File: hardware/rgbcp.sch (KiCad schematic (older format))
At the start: 139 parts, among them SW0 SW_PUSH, SW1 SW_PUSH, SW2 SW_PUSH, SW3 SW_PUSH, SW4 SW_PUSH, SW5 SW_PUSH

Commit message: fix #4: Part List For Schematic
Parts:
- removed U?: MAX603ESA, symbol MAX603ESA
- gave numbers to parts that had none: 70
- renumbered SW0 to B0, SW1 to B1, SW2 to B2, SW3 to B3, SW4 to B4, SW5 to B5, BAT1 to BH1, BAT2 to BH2, BAT3 to BH3, BAT4 to BH4, CXTAL1 to C3, CXTAL2 to C4, DUSB to D1, FETPOL to F1, FETTYP to F2, FETBT1 to F3, FETBT2 to F4, LEDBAT0 to L0, LED0_1 to L0_1, LED0_2 to L0_2, LED0_3 to L0_3, LEDBAT1 to L1, LED1_1 to L1_1, LED1_2 to L1_2, LED1_3 to L1_3, LEDBAT2 to L2, LED2_1 to L2_1, LED2_2 to L2_2, LED2_3 to L2_3, LEDBAT3 to L3, LED3_1 to L3_1, LED3_2 to L3_2, LED3_3 to L3_3, LEDDBG to L4, LED4_1 to L4_1, LED4_2 to L4_2, LED4_3 to L4_3, LED5_1 to L5_1, LED5_2 to L5_2, LED5_3 to L5_3, LED6_1 to L6_1, LED6_2 to L6_2, LED6_3 to L6_3, LED7_1 to L7_1, LED7_2 to L7_2, LED7_3 to L7_3, LED8_1 to L8_1, LED8_2 to L8_2, LED8_3 to L8_3, LED9_1 to L9_1, LED9_2 to L9_2, LED9_3 to L9_3, BJTCS0 to Q0, BJTCS1 to Q1, BJTCS2 to Q2, BJTCS3 to Q3, BJTCS4 to Q4, BJTCS5 to Q5, BJTCS6 to Q6, BJTCS7 to Q7, BJTCS8 to Q8, BJTCS9 to Q9, JUSB to S1, JPBAT to SW1, JPFLAG to SW2, UMCU to U1, ULDO to U2, XTAL to X1
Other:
- note added: "Automatic Power Supply Selector"
- note added: "Battery Level"
- note added: "Debug LEDs"
- note added: "Debug Switches"
- note added: "LEDs for Battery Level"
- note added: "Power Supply (3.3V) for MCU"
- note added: "Power Supply (4V) for all LEDs"
- note added: "Power \nSupply \nStatus"
- note added: "Reverse \nBattery \nProtection"

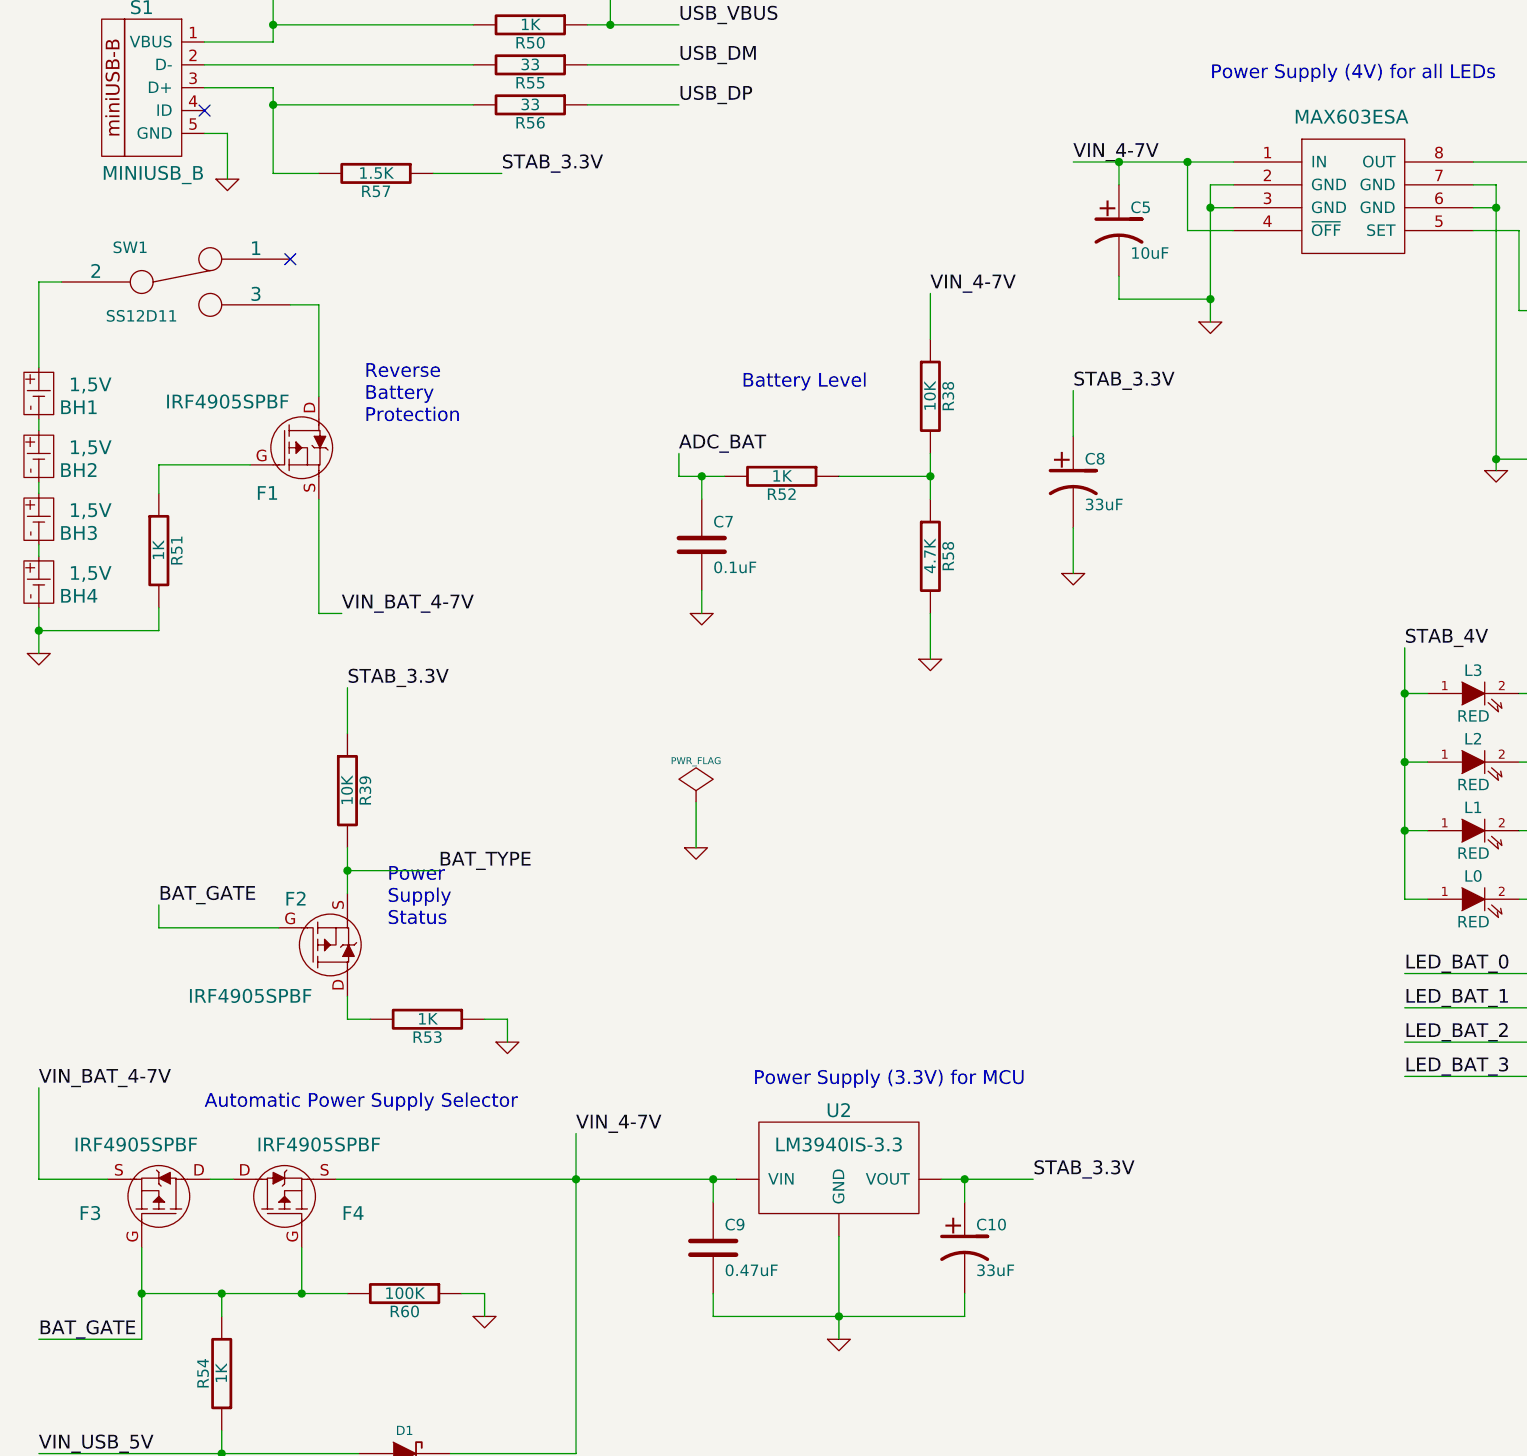
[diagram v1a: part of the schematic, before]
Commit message: fixes #9 Footprints and #25 cvPCB
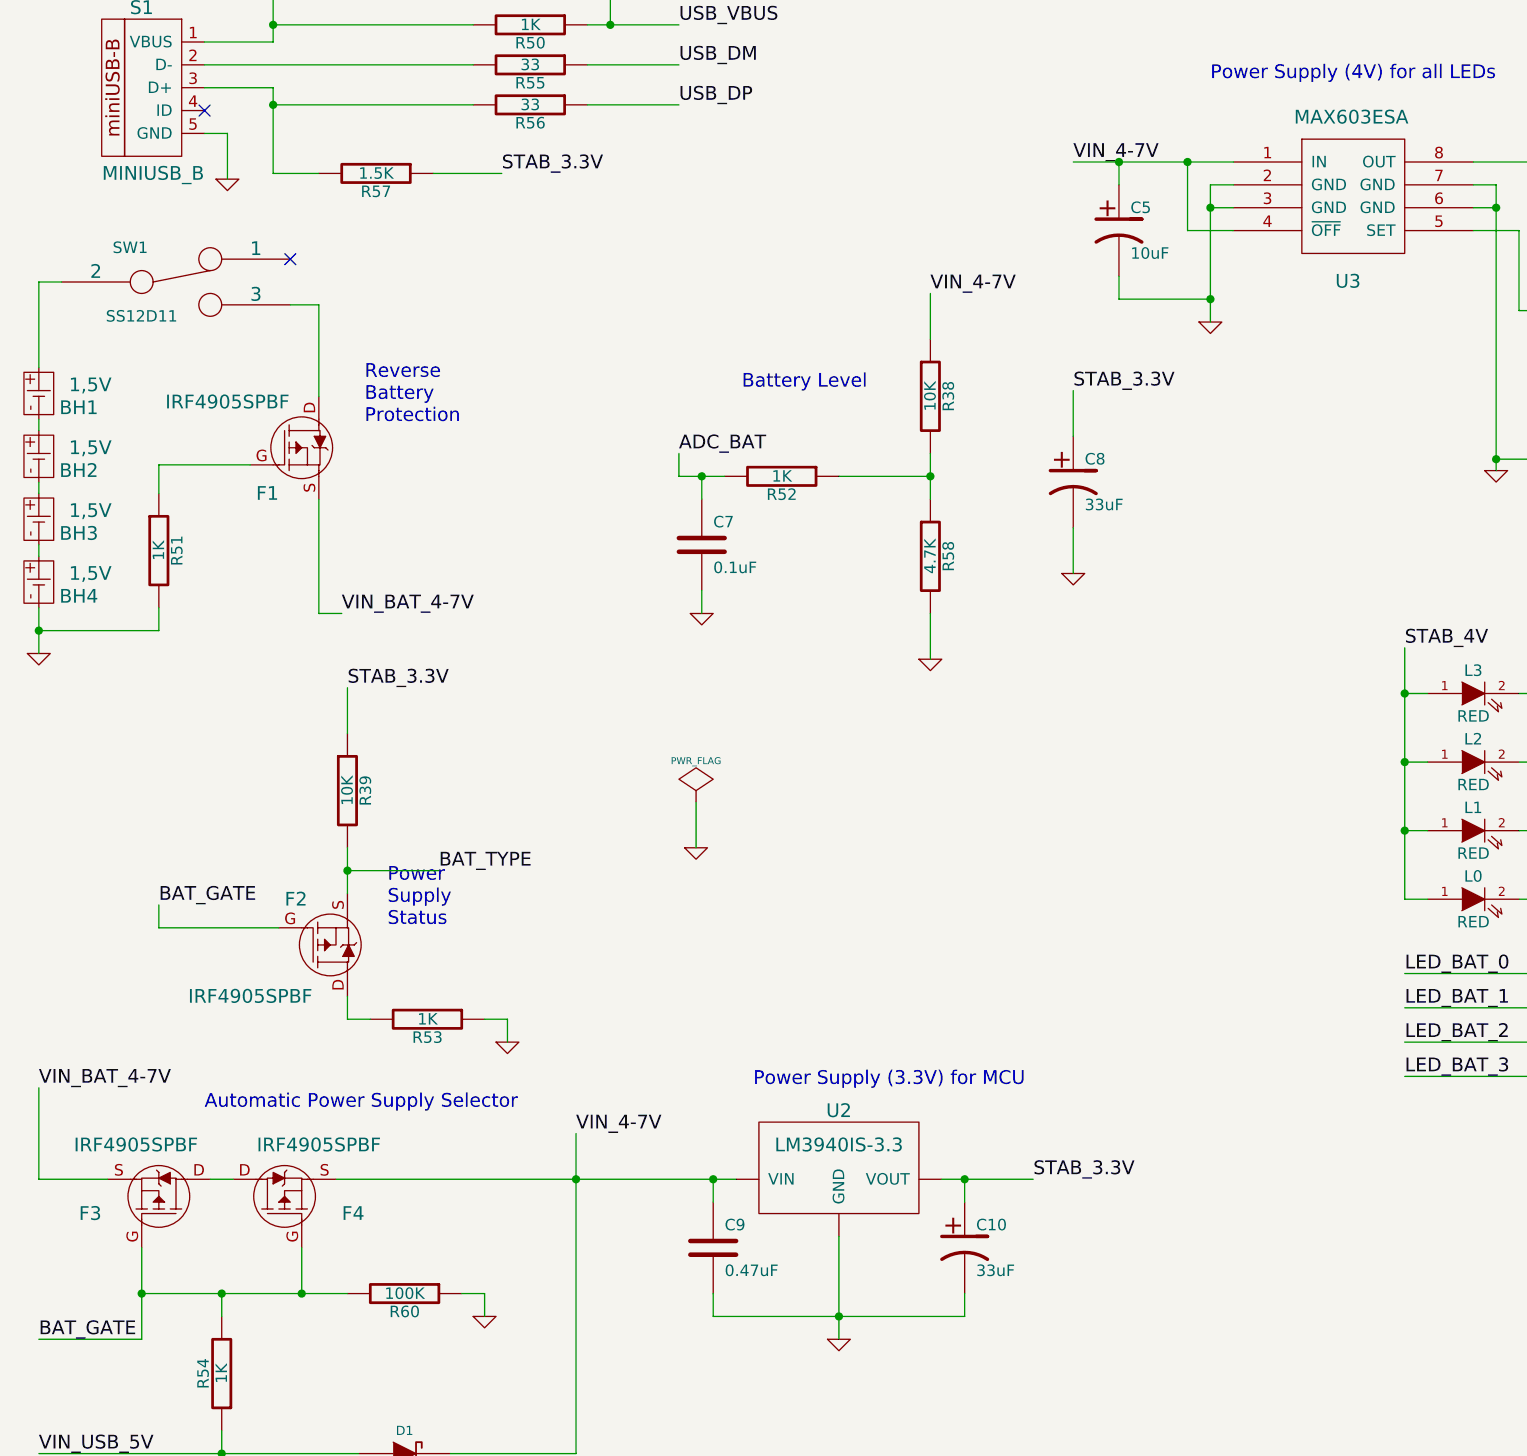
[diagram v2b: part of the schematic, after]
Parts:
- added U3: MAX603ESA, symbol MAX603ESA
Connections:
- net GND: now also U3.2 (GND), U3.3 (GND), U3.6 (GND), U3.7 (GND)
- net STAB_4V: now also U3.8 (OUT)
- net VIN_4-7V: now also U3.1 (IN), U3.4 (~OFF)
- net at R61.1, R62.2: now also U3.5 (SET)
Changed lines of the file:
@@
-EESchema Schematic File Version 2  date Wed 11 Dec 2013 23:25:37 MSK
+EESchema Schematic File Version 2  date Sat 14 Dec 2013 17:15:28 MSK
 LIBS:power
 LIBS:device
@@
 Sheet 1 1
 Title "rgbcp"
-Date "11 dec 2013"
+Date "14 dec 2013"
 Rev "1"
 Comp ""
@@
 Comment4 ""
 $EndDescr
+$Comp
+L MAX603ESA U3
+U 1 1 52AC5722
+P 6350 5550
+F 0 "U3" H 6352 5228 60  0000 C CNN
+F 1 "MAX603ESA" H 6366 5946 60  0000 C CNN
+	1    6350 5550
+	1    0    0    -1
+$EndComp
 Text Notes 7200 7500 0    60   ~ 0
 LEDs for Battery Level
@@
 Connection ~ 5350 5350
 Wire Wire Line
-	5350 5450 5350 5350
+	5350 5350 5350 5450
 Connection ~ 5650 5350
 Wire Wire Line
@@
 	9400 4350 8825 4350
 Wire Wire Line
-	3575 9900 3575 9800
+	3575 9800 3575 9900
 Wire Wire Line
 	11350 10250 11350 8650
@@
 	1850 7325 1950 7325
 Wire Wire Line
-	1775 10100 1775 10300
-Wire Wire Line
-	1075 10300 1975 10300
+	1775 10300 1775 10100
+Wire Wire Line
+	1975 10300 1075 10300
 Connection ~ 1775 10300
 Wire Wire Line
@@
 $EndComp
 $Comp
-L GND #PWR01
+L GND #PWR02
 U 1 1 52A4C090
 P 7000 6700
-F 0 "#PWR01" H 7000 6700 30  0001 C CNN
+F 0 "#PWR02" H 7000 6700 30  0001 C CNN
 F 1 "GND" H 7000 6630 30  0001 C CNN
 	1    7000 6700
@@
 $EndComp
 $Comp
-L GND #PWR02
+L GND #PWR03
 U 1 1 52A4C08B
 P 5750 6050
-F 0 "#PWR02" H 5750 6050 30  0001 C CNN
+F 0 "#PWR03" H 5750 6050 30  0001 C CNN
 F 1 "GND" H 5750 5980 30  0001 C CNN
 	1    5750 6050
@@
 VIN_4-7V
 $Comp
-L MAX603ESA #U03
-U 1 1 52A4BFDB
-P 6350 5550
-F 0 "#U03" H 6402 5278 60  0001 C CNN
-F 1 "MAX603ESA" H 6366 5946 60  0000 C CNN
-	1    6350 5550
-	1    0    0    -1
-$EndComp
-$Comp
 L GND #PWR04

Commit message: fix #25 Fix Footprints
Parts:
- removed U2: LM3940IS-3.3, symbol LM1117DT-3.3
- added U2: LM3940IS-3.3, symbol LM3940IS-3.3
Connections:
- net GND: now also U2.1 (GND)
- net STAB_3.3V: now also U2.2 (VOUT)
- net VIN_4-7V: now also U2.3 (VIN)
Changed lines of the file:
@@
-EESchema Schematic File Version 2  date Sat 14 Dec 2013 17:15:28 MSK
+EESchema Schematic File Version 2  date Sun 15 Dec 2013 12:52:43 MSK
 LIBS:power
 LIBS:device
@@
 Sheet 1 1
 Title "rgbcp"
-Date "14 dec 2013"
+Date "15 dec 2013"
 Rev "1"
 Comp ""
@@
 $EndDescr
 $Comp
+L LM3940IS-3.3 U2
+U 1 1 52AD6CD9
+P 4125 9750
+F 0 "U2" H 4125 10000 60  0000 C CNN
+F 1 "LM3940IS-3.3" H 4125 9850 60  0000 C CNN
+	1    4125 9750
+	1    0    0    -1
+$EndComp
+$Comp
 L MAX603ESA U3
 U 1 1 52AC5722
@@
 	1850 7325 1950 7325
 Wire Wire Line
-	1775 10300 1775 10100
+	1775 10100 1775 10300
 Wire Wire Line
 	1975 10300 1075 10300
@@
 $EndComp
 $Comp
-L GND #PWR02
+L GND #PWR01
 U 1 1 52A4C090
 P 7000 6700
-F 0 "#PWR02" H 7000 6700 30  0001 C CNN
+F 0 "#PWR01" H 7000 6700 30  0001 C CNN
 F 1 "GND" H 7000 6630 30  0001 C CNN
 	1    7000 6700
@@
 $EndComp
 $Comp
-L GND #PWR03
+L GND #PWR02
 U 1 1 52A4C08B
 P 5750 6050
-F 0 "#PWR03" H 5750 6050 30  0001 C CNN
+F 0 "#PWR02" H 5750 6050 30  0001 C CNN
 F 1 "GND" H 5750 5980 30  0001 C CNN
 	1    5750 6050
@@
 VIN_4-7V
 $Comp
-L GND #PWR04
+L GND #PWR03
 U 1 1 522203E1
 P 3500 8350
-F 0 "#PWR04" H 3500 8350 30  0001 C CNN
+F 0 "#PWR03" H 3500 8350 30  0001 C CNN
 F 1 "GND" H 3500 8280 30  0001 C CNN
 	1    3500 8350
@@
 $EndComp
 $Comp
-L PWR_FLAG #FLG05
+L PWR_FLAG #FLG04
 U 1 1 52220139
 P 3500 8150
-F 0 "#FLG05" H 3500 8245 30  0001 C CNN
+F 0 "#FLG04" H 3500 8245 30  0001 C CNN
 F 1 "PWR_FLAG" H 3500 8330 30  0000 C CNN
 	1    3500 8150
@@
 $EndComp
 $Comp
-L GND #PWR06
+L GND #PWR05
 U 1 1 5221BC57
 P 7475 1525
-F 0 "#PWR06" H 7475 1525 30  0001 C CNN
+F 0 "#PWR05" H 7475 1525 30  0001 C CNN
 F 1 "GND" H 7475 1455 30  0001 C CNN
 	1    7475 1525
@@
 $EndComp
 $Comp
-L GND #PWR07
+L GND #PWR06
 U 1 1 5221BC0B
 P 15850 8650
-F 0 "#PWR07" H 15850 8650 30  0001 C CNN
+F 0 "#PWR06" H 15850 8650 30  0001 C CNN
 F 1 "GND" H 15850 8580 30  0001 C CNN
 	1    15850 8650
@@
 $EndComp
 $Comp
-L GND #PWR08
+L GND #PWR07
 U 1 1 52153DFF
 P 3825 4500
-F 0 "#PWR08" H 3825 4500 30  0001 C CNN
+F 0 "#PWR07" H 3825 4500 30  0001 C CNN
 F 1 "GND" H 3825 4430 30  0001 C CNN
 	1    3825 4500
@@
 $EndComp
 $Comp
-L GND #PWR09
+L GND #PWR08
 U 1 1 52153BA3
 P 4525 7525
-F 0 "#PWR09" H 4525 7525 30  0001 C CNN
+F 0 "#PWR08" H 4525 7525 30  0001 C CNN
 F 1 "GND" H 4525 7455 30  0001 C CNN
 	1    4525 7525
@@
 VIN_4-7V
 $Comp
-L GND #PWR010
+L GND #PWR09
 U 1 1 521536AE
 P 3525 7325
-F 0 "#PWR010" H 3525 7325 30  0001 C CNN
+F 0 "#PWR09" H 3525 7325 30  0001 C CNN
 F 1 "GND" H 3525 7255 30  0001 C CNN
 	1    3525 7325
@@
 $EndComp
 $Comp
-L GND #PWR011
+L GND #PWR010
 U 1 1 521535CA
 P 5150 7150
-F 0 "#PWR011" H 5150 7150 30  0001 C CNN
+F 0 "#PWR010" H 5150 7150 30  0001 C CNN
 F 1 "GND" H 5150 7080 30  0001 C CNN
 	1    5150 7150
@@
 STAB_3.3V
 $Comp
-L GND #PWR012
+L GND #PWR011
 U 1 1 521531A9
 P 2675 9200
-F 0 "#PWR012" H 2675 9200 30  0001 C CNN
+F 0 "#PWR011" H 2675 9200 30  0001 C CNN
 F 1 "GND" H 2675 9130 30  0001 C CNN
 	1    2675 9200
@@
 $EndComp
 $Comp
-L GND #PWR013
+L GND #PWR012
 U 1 1 52152A9C
 P 2575 10400
-F 0 "#PWR013" H 2575 10400 30  0001 C CNN
+F 0 "#PWR012" H 2575 10400 30  0001 C CNN
 F 1 "GND" H 2575 10330 30  0001 C CNN
 	1    2575 10400
@@
 NoConn ~ 1350 5125
 $Comp
-L GND #PWR014
+L GND #PWR013
 U 1 1 521524E6
 P 1450 5425
-F 0 "#PWR014" H 1450 5425 30  0001 C CNN
+F 0 "#PWR013" H 1450 5425 30  0001 C CNN
 F 1 "GND" H 1450 5355 30  0001 C CNN
 	1    1450 5425
@@
 ADC_BAT
 $Comp
-L GND #PWR015
+L GND #PWR014
 U 1 1 51FFFE4D
 P 4125 10500
-F 0 "#PWR015" H 4125 10500 30  0001 C CNN
+F 0 "#PWR014" H 4125 10500 30  0001 C CNN
 F 1 "GND" H 4125 10430 30  0001 C CNN
 	1    4125 10500
@@
 $EndComp
 $Comp
-L GND #PWR016
+L GND #PWR015
 U 1 1 51FFF69A
 P 625 7500
-F 0 "#PWR016" H 625 7500 30  0001 C CNN
+F 0 "#PWR015" H 625 7500 30  0001 C CNN
 F 1 "GND" H 625 7430 30  0001 C CNN
 	1    625  7500
@@
 $EndComp
 $Comp
-L GND #PWR017
+L GND #PWR016
 U 1 1 51FECD57
 P 11350 10250
-F 0 "#PWR017" H 11350 10250 30  0001 C CNN
+F 0 "#PWR016" H 11350 10250 30  0001 C CNN
 F 1 "GND" H 11350 10180 30  0001 C CNN
 	1    11350 10250
@@
 DBG_FLAG
 $Comp
-L GND #PWR018
+L GND #PWR017
 U 1 1 51FEC0F4
 P 6550 1525
-F 0 "#PWR018" H 6550 1525 30  0001 C CNN
+F 0 "#PWR017" H 6550 1525 30  0001 C CNN
 F 1 "GND" H 6550 1455 30  0001 C CNN
 	1    6550 1525
@@
 XTALIN
 $Comp
-L GND #PWR019
+L GND #PWR018
 U 1 1 51FEB564
 P 6900 3975
-F 0 "#PWR019" H 6900 3975 30  0001 C CNN
+F 0 "#PWR018" H 6900 3975 30  0001 C CNN
 F 1 "GND" H 6900 3905 30  0001 C CNN
 	1    6900 3975
@@
 	1    0    0    1
 $EndComp
-$Comp
-L LM1117DT-3.3 U2
-U 1 1 51FA0FDC
-P 4125 9750
-F 0 "U2" H 4125 10000 60  0000 C CNN
-F 1 "LM3940IS-3.3" H 4125 9850 60  0000 C CNN
-	1    4125 9750
-	1    0    0    -1
-$EndComp
 $EndSCHEMATC
